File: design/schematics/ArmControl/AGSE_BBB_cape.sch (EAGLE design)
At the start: 49 parts, among them Q1 PFET-FQP27P06, Q2 PFET-FQP27P06, Q3 NFET-FQP30N06L, Q4 NFET-FQP30N06L, Q5 PFET-FQP27P06, Q6 PFET-FQP27P06, Q7 NFET-FQP30N06L, Q8 NFET-FQP30N06L, U1 V_REG_LD1085D2

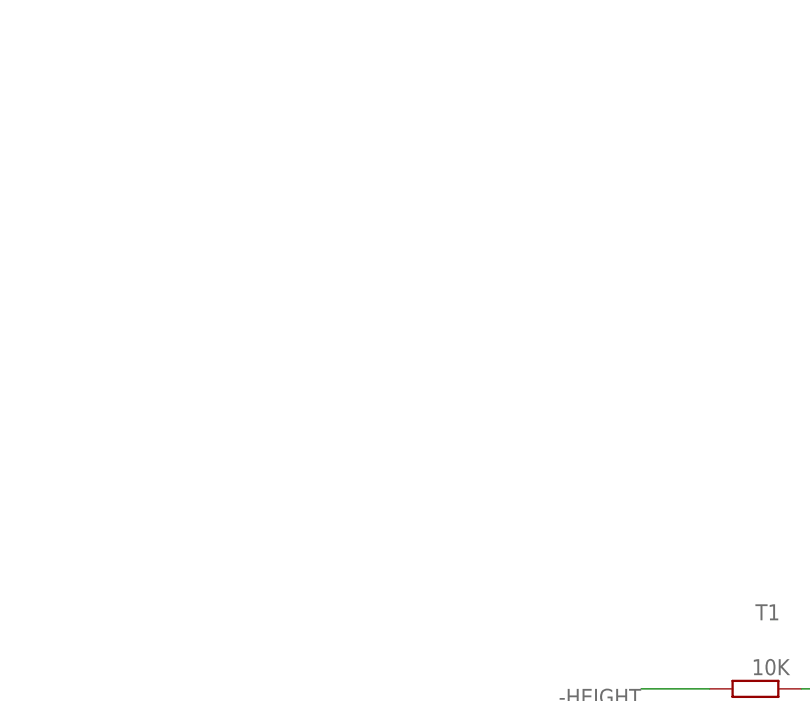
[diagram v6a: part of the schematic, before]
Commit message: Updated board
* added LEDs for the four motor controls
* moved the serial buffer closer to its new pins (closer to the ax-12a
output)
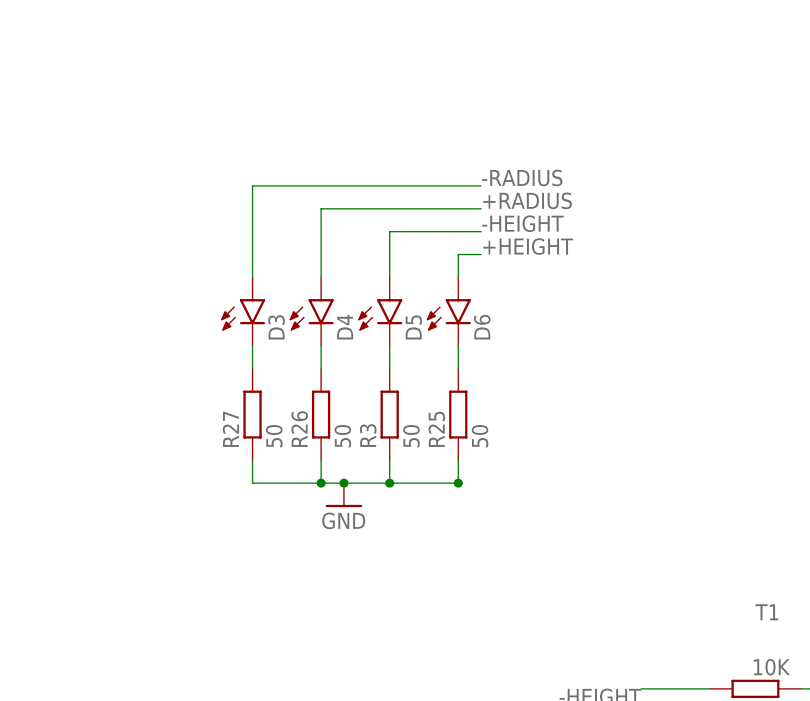
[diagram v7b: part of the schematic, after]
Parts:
- added D3, D4, D5, D6: (no value), SparkFun-LED:LED-FKIT-1206
- added R25, R26, R27, R3: 50, resistor:R-EU_M0805
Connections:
- new net N$1: D3.C, R27.2
- new net N$2: D4.C, R26.2
- new net N$5: D5.C, R3.2
- new net N$6: D6.C, R25.2
- net +HEIGHT: now also D6.A
- net +RADIUS: now also D4.A
- net -HEIGHT: now also D5.A
- net -RADIUS: now also D3.A
- net GND: now also R25.1, R26.1, R27.1, R3.1
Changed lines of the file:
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@@
 <part name="SERVO" library="molex-spox" deviceset="AX-12A" device=""/>
 <part name="GND17" library="supply1" deviceset="GND" device=""/>
+<part name="D3" library="SparkFun-LED" deviceset="LED" device="-FKIT-1206"/>
+<part name="D4" library="SparkFun-LED" deviceset="LED" device="-FKIT-1206"/>
+<part name="D5" library="SparkFun-LED" deviceset="LED" device="-FKIT-1206"/>
+<part name="D6" library="SparkFun-LED" deviceset="LED" device="-FKIT-1206"/>
+<part name="GND2" library="supply1" deviceset="GND" device=""/>
+<part name="R3" library="resistor" deviceset="R-EU_" device="M0805" value="50"/>
+<part name="R25" library="resistor" deviceset="R-EU_" device="M0805" value="50"/>
+<part name="R26" library="resistor" deviceset="R-EU_" device="M0805" value="50"/>
+<part name="R27" library="resistor" deviceset="R-EU_" device="M0805" value="50"/>
 </parts>
 <sheets>
@@
 <instance part="SERVO" gate="G$1" x="180.34" y="111.76"/>
 <instance part="GND17" gate="1" x="167.64" y="106.68"/>
+<instance part="D3" gate="G$1" x="83.82" y="-7.62"/>
+<instance part="D4" gate="G$1" x="91.44" y="-7.62"/>
+<instance part="D5" gate="G$1" x="99.06" y="-7.62"/>
+<instance part="D6" gate="G$1" x="106.68" y="-7.62"/>
+<instance part="GND2" gate="1" x="93.98" y="-30.48"/>
+<instance part="R3" gate="G$1" x="99.06" y="-20.32" rot="R90"/>
+<instance part="R25" gate="G$1" x="106.68" y="-20.32" rot="R90"/>
+<instance part="R26" gate="G$1" x="91.44" y="-20.32" rot="R90"/>
+<instance part="R27" gate="G$1" x="83.82" y="-20.32" rot="R90"/>
 </instances>
 <busses>
@@
 <wire x1="172.72" y1="109.22" x2="167.64" y2="109.22" width="0.1524" layer="91"/>
 <pinref part="GND17" gate="1" pin="GND"/>
+</segment>
+<segment>
+<pinref part="R27" gate="G$1" pin="1"/>
+<pinref part="GND2" gate="1" pin="GND"/>
+<wire x1="83.82" y1="-25.4" x2="83.82" y2="-27.94" width="0.1524" layer="91"/>
+<wire x1="83.82" y1="-27.94" x2="91.44" y2="-27.94" width="0.1524" layer="91"/>
+<pinref part="R26" gate="G$1" pin="1"/>
+<wire x1="91.44" y1="-27.94" x2="93.98" y2="-27.94" width="0.1524" layer="91"/>
+<wire x1="91.44" y1="-25.4" x2="91.44" y2="-27.94" width="0.1524" layer="91"/>
+<pinref part="R3" gate="G$1" pin="1"/>
+<wire x1="99.06" y1="-25.4" x2="99.06" y2="-27.94" width="0.1524" layer="91"/>
+<wire x1="99.06" y1="-27.94" x2="93.98" y2="-27.94" width="0.1524" layer="91"/>
+<pinref part="R25" gate="G$1" pin="1"/>
+<wire x1="106.68" y1="-25.4" x2="106.68" y2="-27.94" width="0.1524" layer="91"/>
+<wire x1="106.68" y1="-27.94" x2="99.06" y2="-27.94" width="0.1524" layer="91"/>
+<junction x="91.44" y="-27.94"/>
+<junction x="93.98" y="-27.94"/>
+<junction x="99.06" y="-27.94"/>
+<junction x="106.68" y="-27.94"/>
 </segment>
 </net>
@@
 <label x="342.9" y="162.56" size="1.778" layer="95"/>
 </segment>
+<segment>
+<pinref part="D5" gate="G$1" pin="A"/>
+<wire x1="99.06" y1="-5.08" x2="99.06" y2="0" width="0.1524" layer="91"/>
+<wire x1="99.06" y1="0" x2="109.22" y2="0" width="0.1524" layer="91"/>
+<label x="109.22" y="0" size="1.778" layer="95"/>
+</segment>
 </net>
 <net name="+HEIGHT" class="0">
@@
 <wire x1="330.2" y1="160.02" x2="342.9" y2="160.02" width="0.1524" layer="91"/>
 <label x="342.9" y="160.02" size="1.778" layer="95"/>
+</segment>
+<segment>
+<pinref part="D6" gate="G$1" pin="A"/>
+<wire x1="106.68" y1="-5.08" x2="106.68" y2="-2.54" width="0.1524" layer="91"/>
+<wire x1="106.68" y1="-2.54" x2="109.22" y2="-2.54" width="0.1524" layer="91"/>
+<label x="109.22" y="-2.54" size="1.778" layer="95"/>
 </segment>
 </net>
@@
 <label x="264.16" y="162.56" size="1.778" layer="95" rot="R180"/>
 </segment>
+<segment>
+<pinref part="D3" gate="G$1" pin="A"/>
+<wire x1="83.82" y1="-5.08" x2="83.82" y2="5.08" width="0.1524" layer="91"/>
+<wire x1="83.82" y1="5.08" x2="109.22" y2="5.08" width="0.1524" layer="91"/>
+<label x="109.22" y="5.08" size="1.778" layer="95"/>
+</segment>
 </net>
 <net name="+RADIUS" class="0">
@@
 <wire x1="274.32" y1="160.02" x2="264.16" y2="160.02" width="0.1524" layer="91"/>
 <label x="264.16" y="160.02" size="1.778" layer="95" rot="R180"/>
+</segment>
+<segment>
+<pinref part="D4" gate="G$1" pin="A"/>
+<wire x1="91.44" y1="-5.08" x2="91.44" y2="2.54" width="0.1524" layer="91"/>
+<wire x1="91.44" y1="2.54" x2="109.22" y2="2.54" width="0.1524" layer="91"/>
+<label x="109.22" y="2.54" size="1.778" layer="95"/>
 </segment>
 </net>
@@
 </segment>
 </net>
+<net name="N$1" class="0">
+<segment>
+<pinref part="D3" gate="G$1" pin="C"/>
+<pinref part="R27" gate="G$1" pin="2"/>
+<wire x1="83.82" y1="-12.7" x2="83.82" y2="-15.24" width="0.1524" layer="91"/>
+</segment>
+</net>
+<net name="N$2" class="0">
+<segment>
+<pinref part="D4" gate="G$1" pin="C"/>
+<pinref part="R26" gate="G$1" pin="2"/>
+<wire x1="91.44" y1="-12.7" x2="91.44" y2="-15.24" width="0.1524" layer="91"/>
+</segment>
+</net>
+<net name="N$5" class="0">
+<segment>
+<pinref part="D5" gate="G$1" pin="C"/>
+<pinref part="R3" gate="G$1" pin="2"/>
+<wire x1="99.06" y1="-12.7" x2="99.06" y2="-15.24" width="0.1524" layer="91"/>
+</segment>
+</net>
+<net name="N$6" class="0">
+<segment>
+<pinref part="D6" gate="G$1" pin="C"/>
+<pinref part="R25" gate="G$1" pin="2"/>
+<wire x1="106.68" y1="-12.7" x2="106.68" y2="-15.24" width="0.1524" layer="91"/>
+</segment>
+</net>
